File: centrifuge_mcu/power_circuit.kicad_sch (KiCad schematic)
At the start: 64 parts, among them J108 USB_B_Micro, J109 Barrel_Jack, J110 PowerIn, J111 PowerPads, Q101 Q_PMOS_DGS, U102 TPS54294, U103 TPS54294, U104 TPS54294

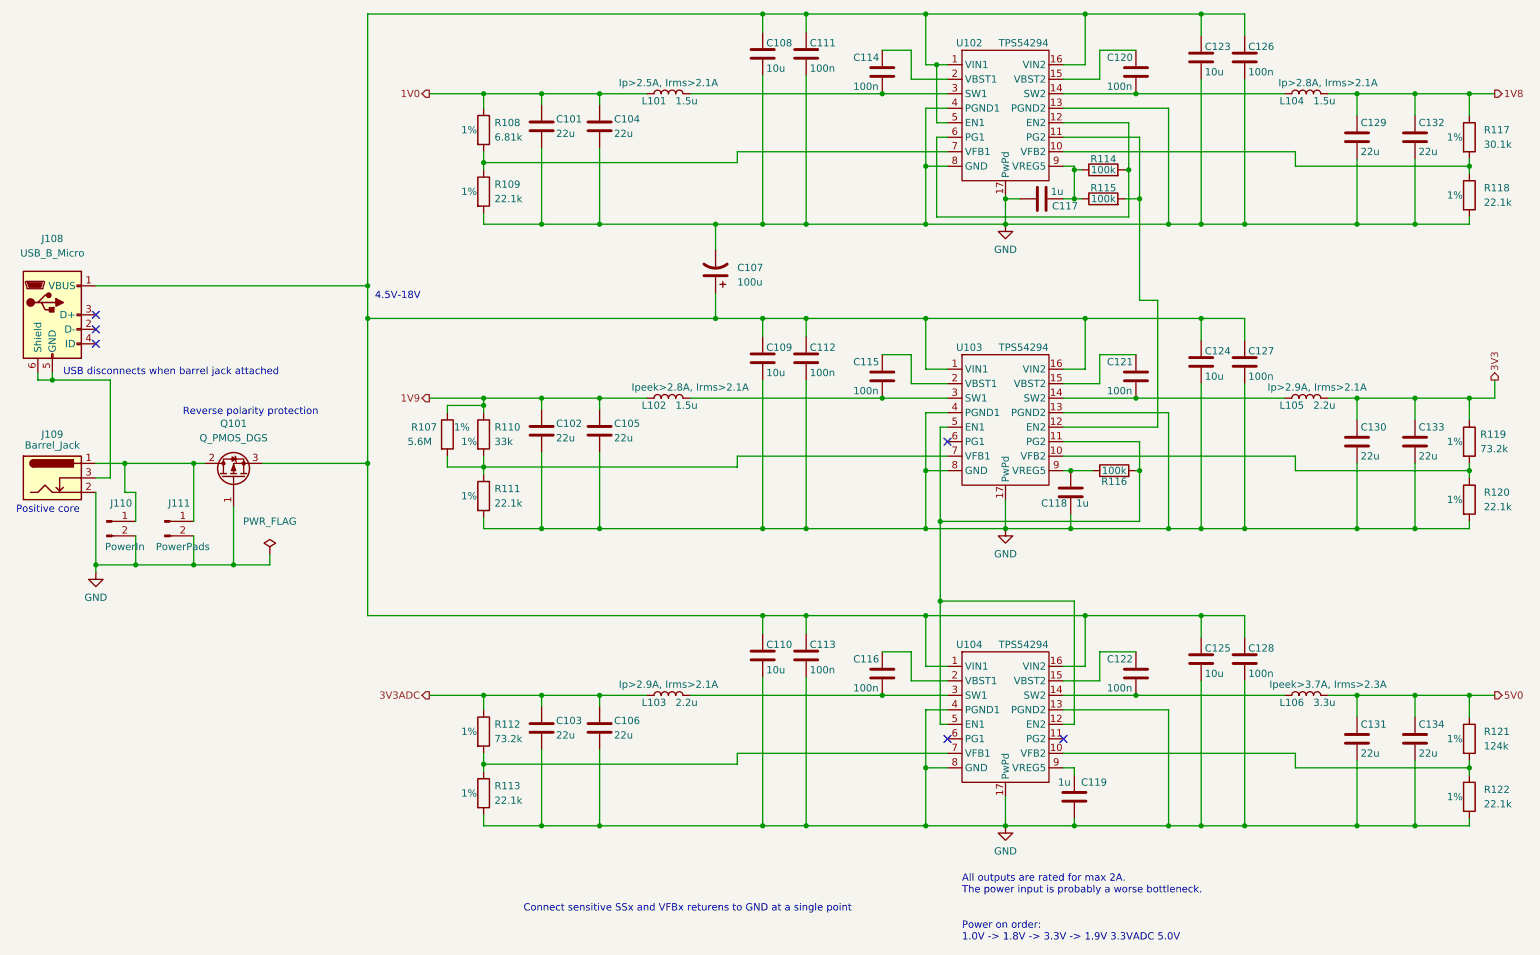
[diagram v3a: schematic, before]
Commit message: start routing PCB for the MCU, starting with power
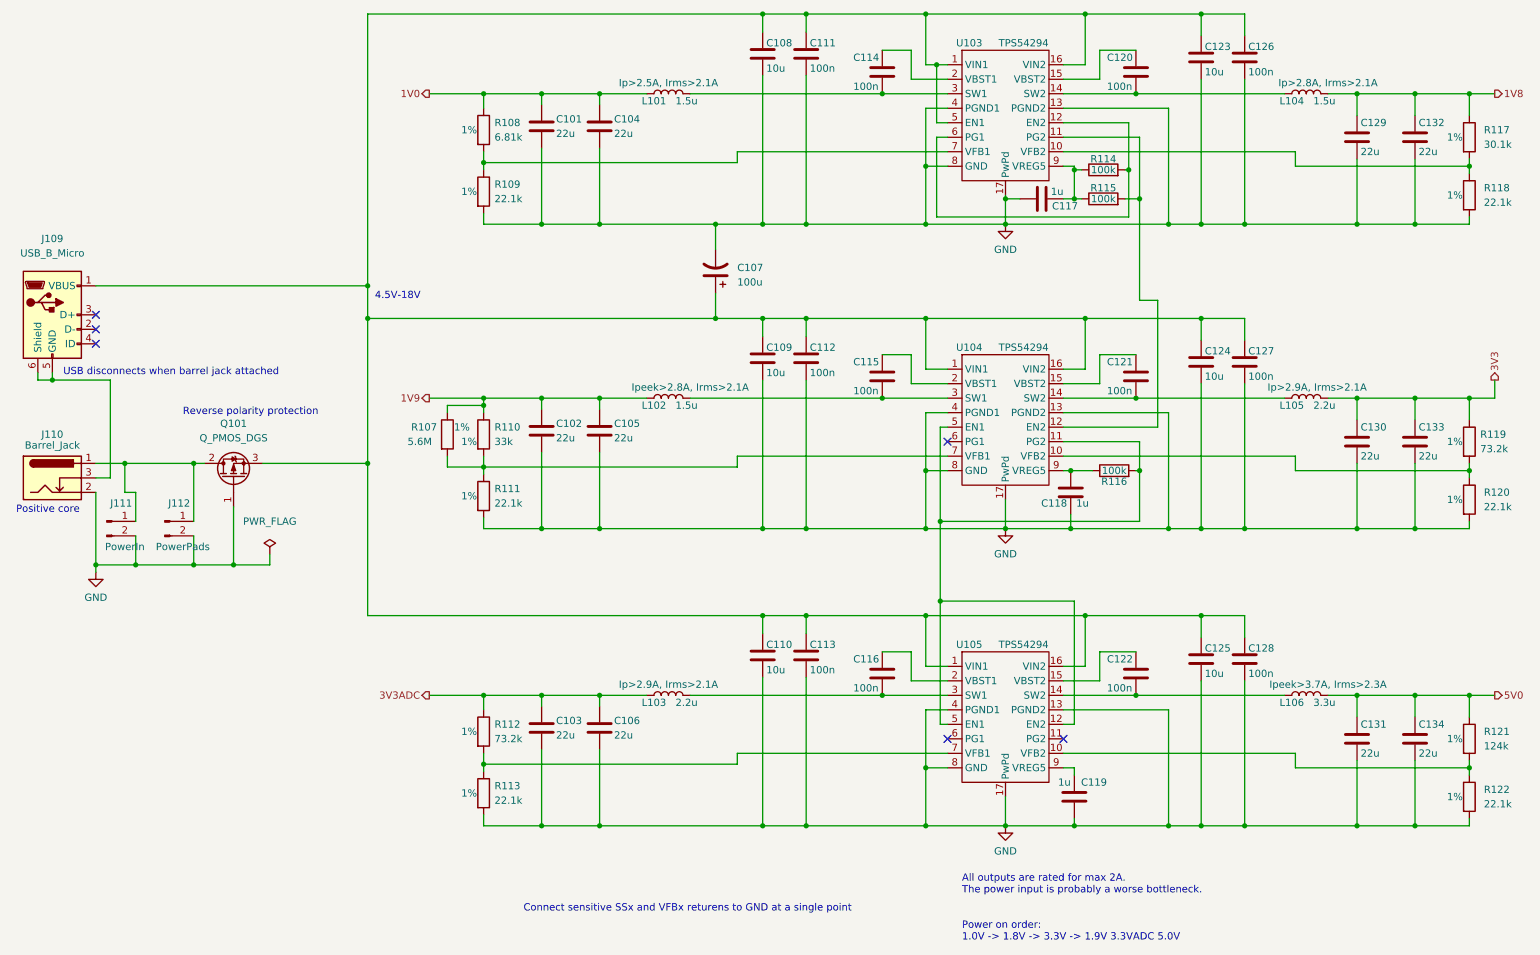
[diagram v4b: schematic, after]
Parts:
- renumbered J108 to J109, J109 to J110, J110 to J111, J111 to J112, U102 to U103, U103 to U104, U104 to U105
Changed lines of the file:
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@@
   (symbol (lib_id "Connector:Conn_01x02_Male") (at 38.735 105.41 0) (unit 1)
     (in_bom yes) (on_board yes)
-    (property "Reference" "J111" (id 0) (at 41.275 102.235 0))
+    (property "Reference" "J112" (id 0) (at 41.275 102.235 0))
     (property "Value" "PowerPads" (id 1) (at 41.91 109.855 0))
     (property "Footprint" "centrifuge_mcu:PowerPads" (id 2) (at 38.735 105.41 0)
@@
   (symbol (lib_name "TPS54294_2") (lib_id "mcu_centrifuge_library:TPS54294") (at 186.055 87.63 0) (unit 1)
     (in_bom yes) (on_board yes)
-    (property "Reference" "U103" (id 0) (at 179.705 74.93 0))
+    (property "Reference" "U104" (id 0) (at 179.705 74.93 0))
     (property "Value" "TPS54294" (id 1) (at 189.23 74.93 0))
     (property "Footprint" "centrifuge_mcu:TSSOP-16-1EP_4.4x5mm_P0.65mm_EP3x3mm_ThermalVias_EXTRA" (id 2) (at 188.595 96.52 0)
@@
   (symbol (lib_id "Connector:Barrel_Jack_Switch") (at 19.05 97.79 0) (unit 1)
     (in_bom yes) (on_board yes)
-    (property "Reference" "J109" (id 0) (at 19.05 90.17 0))
+    (property "Reference" "J110" (id 0) (at 19.05 90.17 0))
     (property "Value" "Barrel_Jack" (id 1) (at 19.05 92.075 0))
     (property "Footprint" "Connector_BarrelJack:BarrelJack_CUI_PJ-102AH_Horizontal" (id 2) (at 20.32 98.806 0)
@@
   (symbol (lib_id "Connector:USB_B_Micro") (at 19.05 69.215 0) (unit 1)
     (in_bom yes) (on_board yes) (fields_autoplaced)
-    (property "Reference" "J108" (id 0) (at 19.05 55.88 0))
+    (property "Reference" "J109" (id 0) (at 19.05 55.88 0))
     (property "Value" "USB_B_Micro" (id 1) (at 19.05 58.42 0))
     (property "Footprint" "Connector_USB:USB_Micro-B_Molex-105017-0001" (id 2) (at 22.86 70.485 0)
@@
   (symbol (lib_id "mcu_centrifuge_library:TPS54294") (at 186.055 139.7 0) (unit 1)
     (in_bom yes) (on_board yes)
-    (property "Reference" "U104" (id 0) (at 179.705 127 0))
+    (property "Reference" "U105" (id 0) (at 179.705 127 0))
     (property "Value" "TPS54294" (id 1) (at 189.23 127 0))
     (property "Footprint" "centrifuge_mcu:TSSOP-16-1EP_4.4x5mm_P0.65mm_EP3x3mm_ThermalVias_EXTRA" (id 2) (at 188.595 148.59 0)
@@
   (symbol (lib_id "Connector:Conn_01x02_Male") (at 28.575 105.41 0) (unit 1)
     (in_bom yes) (on_board yes)
-    (property "Reference" "J110" (id 0) (at 31.115 102.235 0))
+    (property "Reference" "J111" (id 0) (at 31.115 102.235 0))
     (property "Value" "PowerIn" (id 1) (at 31.75 109.855 0))
     (property "Footprint" "Connector_PinHeader_2.54mm:PinHeader_1x02_P2.54mm_Vertical" (id 2) (at 28.575 105.41 0)
@@
   (symbol (lib_name "TPS54294_1") (lib_id "mcu_centrifuge_library:TPS54294") (at 186.055 34.29 0) (unit 1)
     (in_bom yes) (on_board yes)
-    (property "Reference" "U102" (id 0) (at 179.705 21.59 0))
+    (property "Reference" "U103" (id 0) (at 179.705 21.59 0))
     (property "Value" "TPS54294" (id 1) (at 189.23 21.59 0))
     (property "Footprint" "centrifuge_mcu:TSSOP-16-1EP_4.4x5mm_P0.65mm_EP3x3mm_ThermalVias_EXTRA" (id 2) (at 188.595 59.69 0)

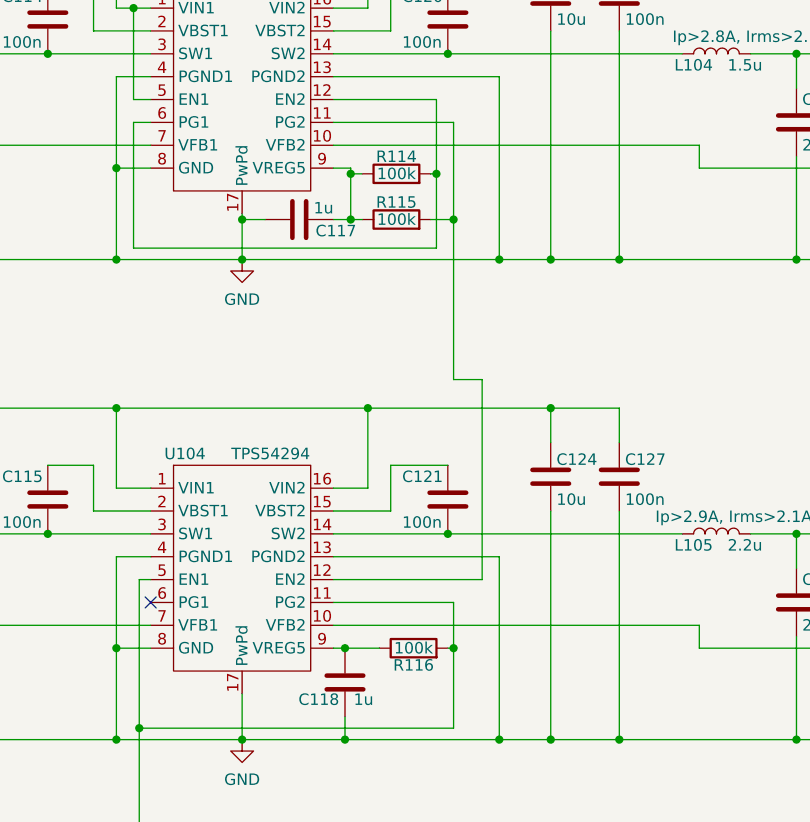
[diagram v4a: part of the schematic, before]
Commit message: connect everything in MCU pcb, connection time
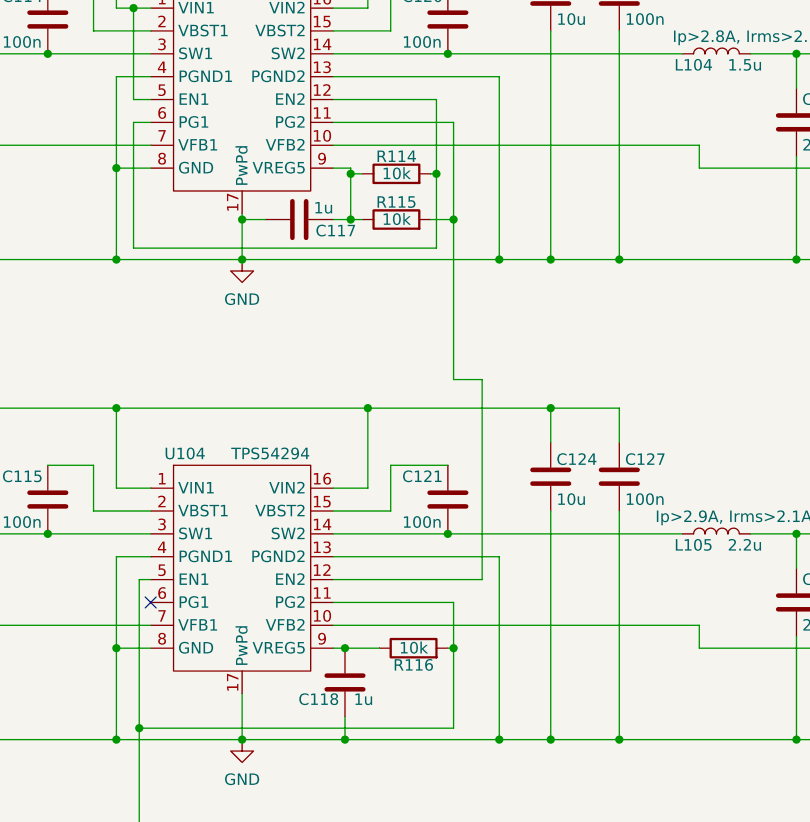
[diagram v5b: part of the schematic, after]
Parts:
- R114, R115: value 100k -> 10k
- R116: value 100k -> 10k; Purchase https://www.digikey.no/no/products/detail/yageo/AC0805FR-07100KL/5896520 -> https://www.digikey.no/no/products/detail/yageo/AC0805FR-0710KL/2827834
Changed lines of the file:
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@@
     (in_bom yes) (on_board yes)
     (property "Reference" "R114" (id 0) (at 203.2 41.91 90))
-    (property "Value" "100k" (id 1) (at 203.2 43.815 90))
+    (property "Value" "10k" (id 1) (at 203.2 43.815 90))
     (property "Footprint" "Resistor_SMD:R_0805_2012Metric_Pad1.20x1.40mm_HandSolder" (id 2) (at 203.2 45.593 90)
       (effects (font (size 1.27 1.27)) hide)
@@
     (in_bom yes) (on_board yes)
     (property "Reference" "R116" (id 0) (at 205.105 98.425 90))
-    (property "Value" "100k" (id 1) (at 205.105 96.52 90))
+    (property "Value" "10k" (id 1) (at 205.105 96.52 90))
     (property "Footprint" "Resistor_SMD:R_0805_2012Metric_Pad1.20x1.40mm_HandSolder" (id 2) (at 205.105 98.298 90)
       (effects (font (size 1.27 1.27)) hide)
@@
       (effects (font (size 1.27 1.27)) hide)
     )
-    (property "Purchase" "https://www.digikey.no/no/products/detail/yageo/AC0805FR-07100KL/5896520" (id 4) (at 205.105 96.52 0)
+    (property "Purchase" "https://www.digikey.no/no/products/detail/yageo/AC0805FR-0710KL/2827834" (id 4) (at 205.105 96.52 0)
       (effects (font (size 1.27 1.27)) hide)
     )
@@
     (in_bom yes) (on_board yes)
     (property "Reference" "R115" (id 0) (at 203.2 46.99 90))
-    (property "Value" "100k" (id 1) (at 203.2 48.895 90))
+    (property "Value" "10k" (id 1) (at 203.2 48.895 90))
     (property "Footprint" "Resistor_SMD:R_0805_2012Metric_Pad1.20x1.40mm_HandSolder" (id 2) (at 203.2 50.673 90)
       (effects (font (size 1.27 1.27)) hide)
